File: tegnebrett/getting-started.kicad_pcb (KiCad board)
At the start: 2 copper layers, 15 parts, among them J1 FH12-45S-0.5SH55, J2 FH12-6S-1SH55, J3 Conn_ST_STDC14, J4 DA15_Socket, J5 MCU_Header_Pin, J6 FPGA_Header_Pin, J8 USB-A1HSW6, U1 XC7A100T-2FTG256I, U2 Oscillator 100MHz, U3 TPS54294PWP1, U4 TPS54294PWP2, U5 STM32U5G7VJTxQ, U6 VGA Transceiver, U7 VGA Transciever, U8 IS66WVH16M8DBLL-100B1LI1

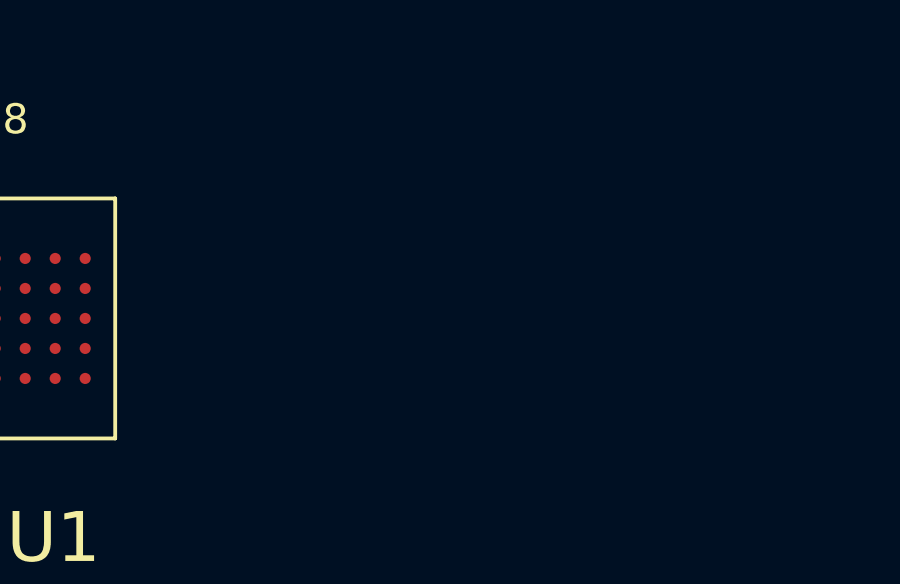
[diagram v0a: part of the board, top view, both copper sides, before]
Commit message: feat: add FPGA flash footprint, import to PCB
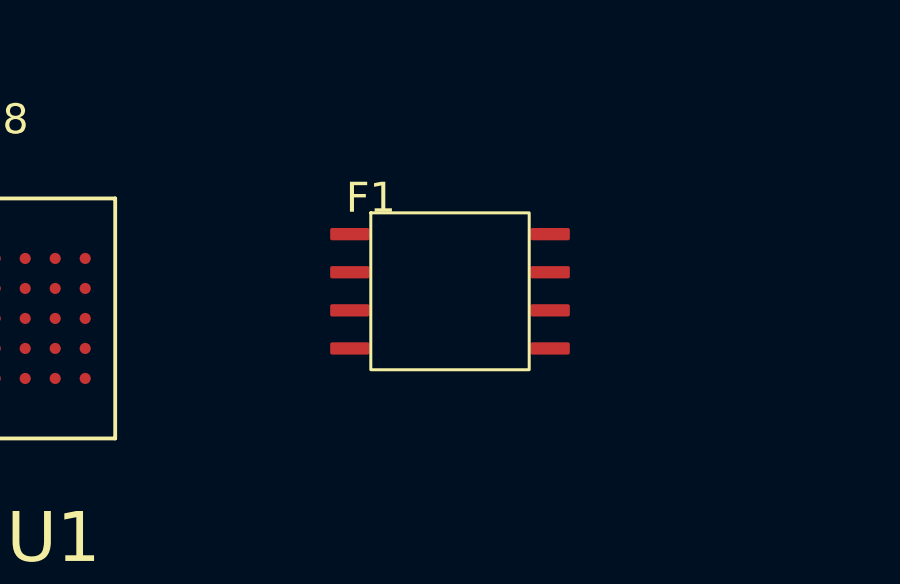
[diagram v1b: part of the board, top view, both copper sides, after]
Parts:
- added F1: GD25F128FS2GR1, tegnebrett_modules:flash_tegnebrett, F.Cu at (54.5, 18.0)
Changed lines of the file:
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@@
 	(net 205 "unconnected-(U1A-IO_L14P_T2_SRCC_14-PadP10)")
 	(net 206 "Net-(U1A-IO_L24P_T3_RS1_15)")
-	(net 207 "Net-(GD25F128FS2GR1-SCLK)")
+	(net 207 "Net-(F1-SI(IO0))")
 	(net 208 "Net-(U1C-TDO_0)")
-	(net 209 "Net-(GD25F128FS2GR1-IO3)")
+	(net 209 "Net-(F1-IO3)")
 	(net 210 "unconnected-(U1B-IO_L4N_T0_34-PadP1)")
 	(net 211 "unconnected-(U1B-IO_L6N_T0_VREF_34-PadN4)")
@@
 	(net 237 "unconnected-(U1B-IO_L22N_T3_35-PadJ1)")
 	(net 238 "unconnected-(U1B-IO_L2P_T0_34-PadM2)")
-	(net 239 "Net-(GD25F128FS2GR1-IO2)")
+	(net 239 "Net-(F1-SCLK)")
 	(net 240 "unconnected-(U1B-IO_L16N_T2_35-PadG4)")
 	(net 241 "unconnected-(U1B-IO_L13P_T2_MRCC_35-PadF5)")
@@
 	(net 249 "unconnected-(U1B-IO_L10P_T1_34-PadP5)")
 	(net 250 "unconnected-(U1A-IO_L3N_T0_DQS_EMCCLK_14-PadM15)")
-	(net 251 "Net-(GD25F128FS2GR1-SO1(IO1))")
+	(net 251 "Net-(F1-SO1(IO1))")
 	(net 252 "unconnected-(U1A-IO_L5P_T0_AD9P_15-PadB12)")
 	(net 253 "Net-(U1C-TMS_0)")
@@
 	(net 326 "Net-(U1C-INIT_B_0)")
 	(net 327 "unconnected-(U1A-IO_L8N_T1_AD10N_15-PadB14)")
-	(net 328 "Net-(GD25F128FS2GR1-SI(IO0))")
+	(net 328 "Net-(F1-IO2)")
 	(footprint "Connector_PinHeader_1.27mm:PinHeader_2x07_P1.27mm_Vertical"
 		(layer "F.Cu")
@@
 			(size 0.5 0.5)
 			(layers "F.Cu" "F.Mask" "F.Paste")
-			(net 207 "Net-(GD25F128FS2GR1-SCLK)")
+			(net 239 "Net-(F1-SCLK)")
 			(pinfunction "CCLK_0")
 			(pintype "bidirectional")
@@
 			(size 0.5 0.5)
 			(layers "F.Cu" "F.Mask" "F.Paste")
-			(net 328 "Net-(GD25F128FS2GR1-SI(IO0))")
+			(net 207 "Net-(F1-SI(IO0))")
 			(pinfunction "IO_L1P_T0_D00_MOSI_14")
 			(pintype "bidirectional")
@@
 			(size 0.5 0.5)
 			(layers "F.Cu" "F.Mask" "F.Paste")
-			(net 251 "Net-(GD25F128FS2GR1-SO1(IO1))")
+			(net 251 "Net-(F1-SO1(IO1))")
 			(pinfunction "IO_L1N_T0_D01_DIN_14")
 			(pintype "bidirectional")
@@
 			(size 0.5 0.5)
 			(layers "F.Cu" "F.Mask" "F.Paste")
-			(net 239 "Net-(GD25F128FS2GR1-IO2)")
+			(net 328 "Net-(F1-IO2)")
 			(pinfunction "IO_L2P_T0_D02_14")
 			(pintype "bidirectional")
@@
 			(size 0.5 0.5)
 			(layers "F.Cu" "F.Mask" "F.Paste")
-			(net 209 "Net-(GD25F128FS2GR1-IO3)")
+			(net 209 "Net-(F1-IO3)")
 			(pinfunction "IO_L2N_T0_D03_14")
 			(pintype "bidirectional")
@@
 		)
 	)
+	(footprint "tegnebrett_modules:flash_tegnebrett"
+		(layer "F.Cu")
+		(at 54.52 17.98)
+		(property "Reference" "F1"
+			(at 0 -0.5 0)
+			(unlocked yes)
+			(layer "F.SilkS")
+			(effects
+				(font
+					(size 1 1)
+					(thickness 0.1)
+				)
+			)
+		)
+		(property "Value" "GD25F128FS2GR1"
+			(at 0 1 0)
+			(unlocked yes)
+			(layer "F.Fab")
+			(effects
+				(font
+					(size 1 1)
+					(thickness 0.15)
+				)
+			)
+		)
+		(property "Datasheet" ""
+			(at 0 0 0)
+			(unlocked yes)
+			(layer "F.Fab")
+			(hide yes)
+			(effects
+				(font
+					(size 1 1)
+					(thickness 0.15)
+				)
+			)
+		)
+		(property "Description" ""
+			(at 0 0 0)
+			(unlocked yes)
+			(layer "F.Fab")
+			(hide yes)
+			(effects
+				(font
+					(size 1 1)
+					(thickness 0.15)
+				)
+			)
+		)
+		(sheetname "/FPGA/")
+		(sheetfile "debug.kicad_sch")
+		(attr smd)
+		(fp_rect
+			(start 0 0)
+			(end 5.28 5.23)
+			(stroke
+				(width 0.1)
+				(type solid)
+			)
+			(fill no)
+			(layer "F.SilkS")
+		)
+		(fp_text user "${REFERENCE}"
+			(at 0 2.5 0)
+			(unlocked yes)
+			(layer "F.Fab")
+			(effects
+				(font
+					(size 1 1)
+					(thickness 0.15)
+				)
+			)
+		)
+		(pad "1" smd roundrect
+			(at -0.7 0.71)
+			(size 1.31 0.41)
+			(layers "F.Cu" "F.Mask" "F.Paste")
+			(roundrect_rratio 0.15)
+			(net 302 "/FPGA/CS#")
+			(pinfunction "CS#")
+			(pintype "input")
+		)
+		(pad "2" smd roundrect
+			(at -0.7 1.98)
+			(size 1.31 0.41)
+			(layers "F.Cu" "F.Mask" "F.Paste")
+			(roundrect_rratio 0.15)
+			(net 251 "Net-(F1-SO1(IO1))")
+			(pinfunction "SO1(IO1)")
+			(pintype "bidirectional")
+		)
+		(pad "3" smd roundrect
+			(at -0.7 3.25)
+			(size 1.31 0.41)
+			(layers "F.Cu" "F.Mask" "F.Paste")
+			(roundrect_rratio 0.15)
+			(net 328 "Net-(F1-IO2)")
+			(pinfunction "IO2")
+			(pintype "bidirectional")
+		)
+		(pad "4" smd roundrect
+			(at -0.7 4.52)
+			(size 1.31 0.41)
+			(layers "F.Cu" "F.Mask" "F.Paste")
+			(roundrect_rratio 0.15)
+			(net 1 "GND")
+			(pinfunction "VSS")
+			(pintype "power_in")
+		)
+		(pad "5" smd roundrect
+			(at 5.98 4.52)
+			(size 1.31 0.41)
+			(layers "F.Cu" "F.Mask" "F.Paste")
+			(roundrect_rratio 0.15)
+			(net 207 "Net-(F1-SI(IO0))")
+			(pinfunction "SI(IO0)")
+			(pintype "bidirectional")
+		)
+		(pad "6" smd roundrect
+			(at 5.98 3.25)
+			(size 1.31 0.41)
+			(layers "F.Cu" "F.Mask" "F.Paste")
+			(roundrect_rratio 0.15)
+			(net 239 "Net-(F1-SCLK)")
+			(pinfunction "SCLK")
+			(pintype "input")
+		)
+		(pad "7" smd roundrect
+			(at 5.98 1.98)
+			(size 1.31 0.41)
+			(layers "F.Cu" "F.Mask" "F.Paste")
+			(roundrect_rratio 0.15)
+			(net 209 "Net-(F1-IO3)")
+			(pinfunction "IO3")
+			(pintype "bidirectional")
+		)
+		(pad "8" smd roundrect
+			(at 5.98 0.71)
+			(size 1.31 0.41)
+			(layers "F.Cu" "F.Mask" "F.Paste")
+			(roundrect_rratio 0.15)
+			(net 16 "+3V3")
+			(pinfunction "VCC")
+			(pintype "power_in")
+		)
+		(embedded_fonts no)
+	)
 	(footprint "tegnebrett_modules:psram"

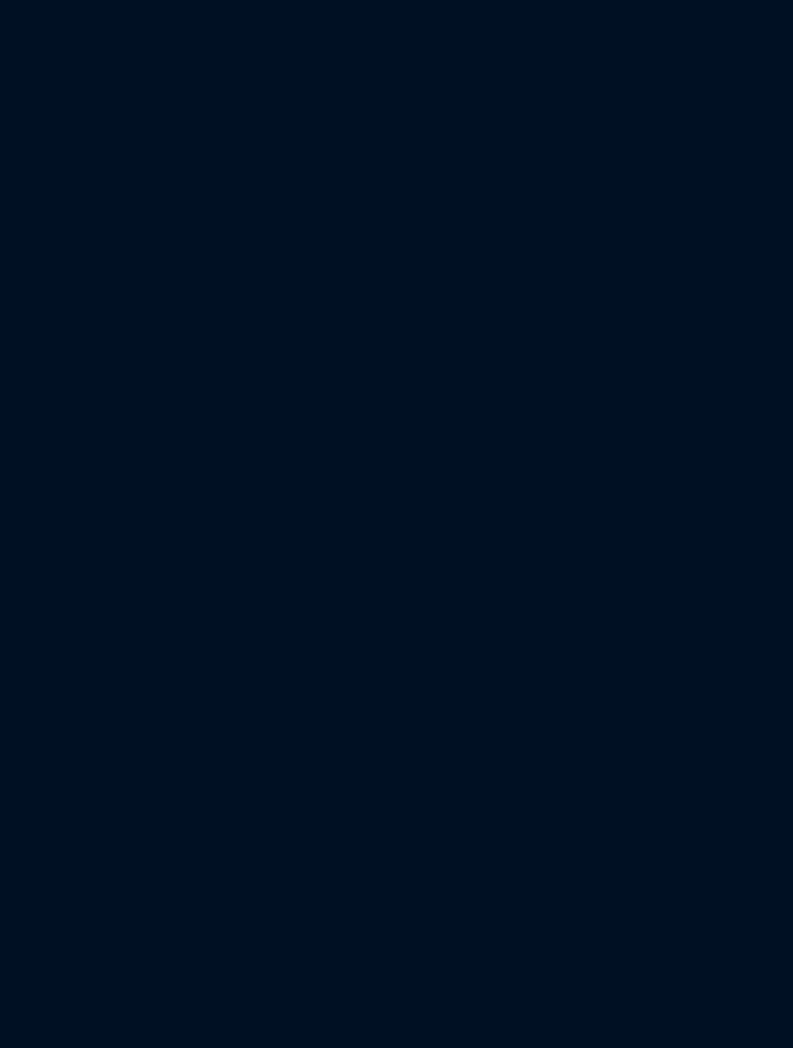
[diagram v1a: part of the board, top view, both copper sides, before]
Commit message: feat: add LED footprint, and add them to PCB
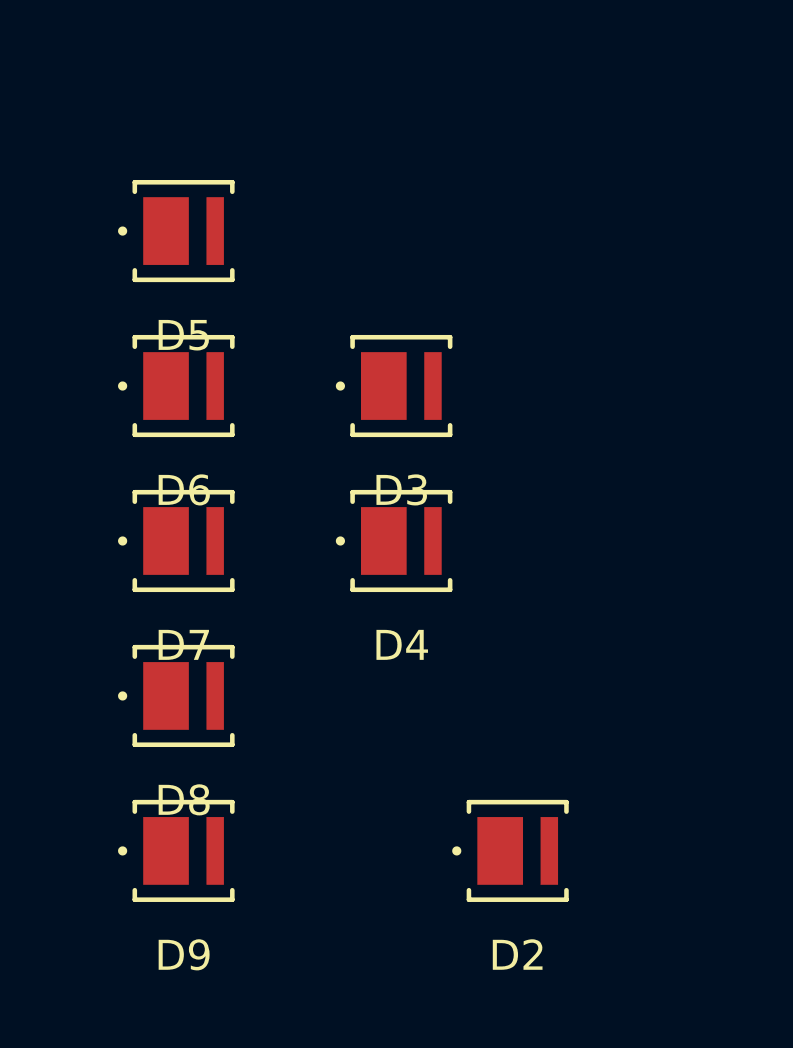
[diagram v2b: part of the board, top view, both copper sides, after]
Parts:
- added D2: LED, tegnebrett_modules:LED_J-SERIES_3030_CRW-M, F.Cu at (28.6, 192.5)
- added D3: LED, tegnebrett_modules:LED_J-SERIES_3030_CRW-M, F.Cu at (24.7, 177.0)
- added D4: LED, tegnebrett_modules:LED_J-SERIES_3030_CRW-M, F.Cu at (24.7, 182.2)
- added D5: LED, tegnebrett_modules:LED_J-SERIES_3030_CRW-M, F.Cu at (17.4, 171.8)
- added D6: LED, tegnebrett_modules:LED_J-SERIES_3030_CRW-M, F.Cu at (17.4, 177.0)
- added D7: LED, tegnebrett_modules:LED_J-SERIES_3030_CRW-M, F.Cu at (17.4, 182.2)
- added D8: LED, tegnebrett_modules:LED_J-SERIES_3030_CRW-M, F.Cu at (17.4, 187.3)
- added D9: LED, tegnebrett_modules:LED_J-SERIES_3030_CRW-M, F.Cu at (17.4, 192.5)

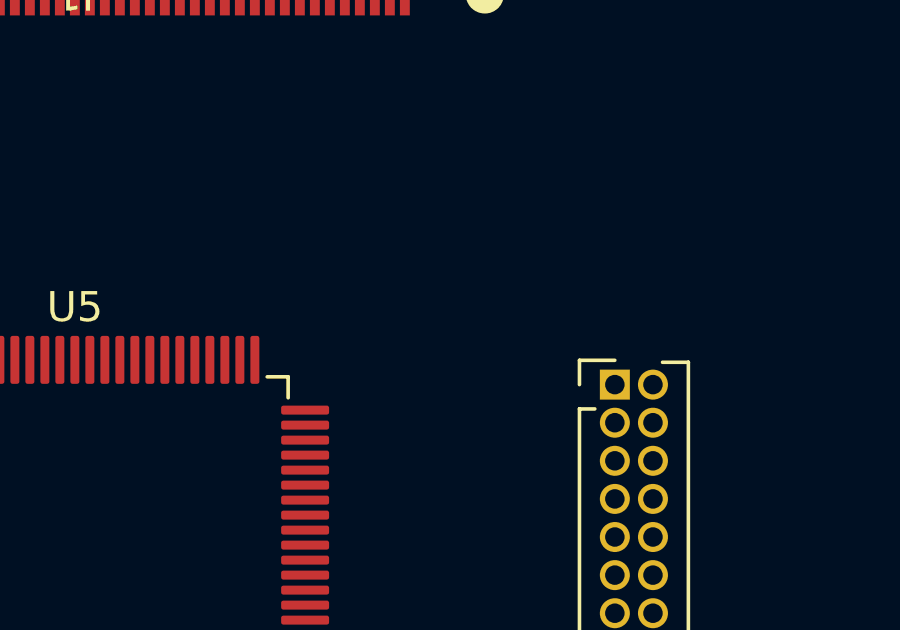
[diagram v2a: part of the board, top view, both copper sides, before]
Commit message: feat: add 48MHz crystal footprint + add to PCB
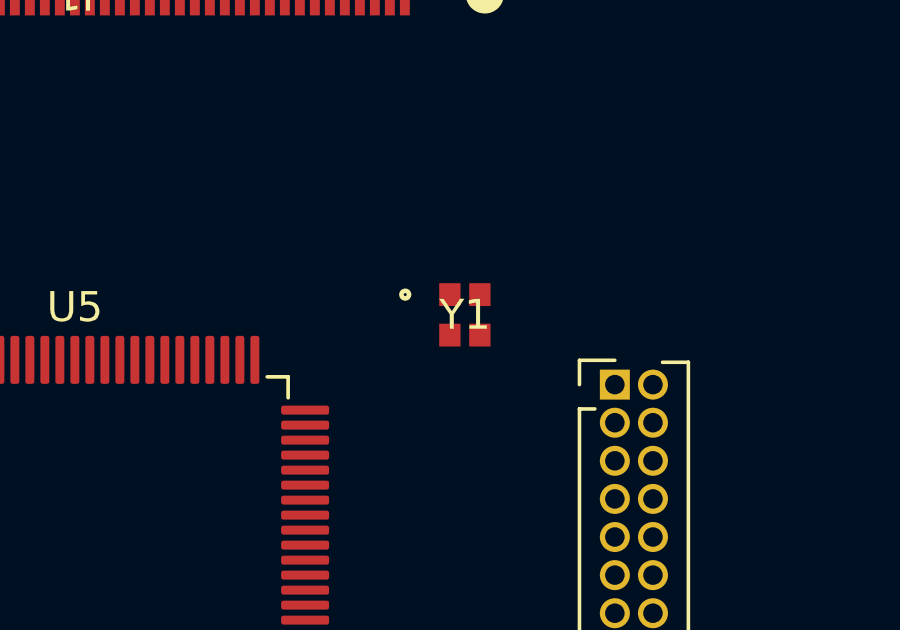
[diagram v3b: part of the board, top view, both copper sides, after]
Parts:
- added Y1: 48MHz, tegnebrett_modules:XRCGB48M000F4M00R0_MUR, F.Cu at (211.5, 112.8)

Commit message: feat: add inductors and capacitors to PCB
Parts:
- added C1: 47u, Capacitor_SMD:C_0805_2012Metric_Pad1.18x1.45mm_HandSolder, F.Cu at (123.3, 146.9)
- added C10: 4u7, Capacitor_SMD:C_0805_2012Metric_Pad1.18x1.45mm_HandSolder, F.Cu at (123.3, 162.0)
- added C100: 100n, Capacitor_SMD:C_0805_2012Metric_Pad1.18x1.45mm_HandSolder, F.Cu at (150.6, 168.0)
- added C101: 22u, Capacitor_SMD:C_1206_3216Metric_Pad1.33x1.80mm_HandSolder, F.Cu at (162.0, 153.8)
- added C102: 22u, Capacitor_SMD:C_1206_3216Metric_Pad1.33x1.80mm_HandSolder, F.Cu at (162.0, 157.2)
- added C103: 22u, Capacitor_SMD:C_1206_3216Metric_Pad1.33x1.80mm_HandSolder, F.Cu at (162.0, 160.5)
- added C104: 10u, Capacitor_SMD:C_1206_3216Metric_Pad1.33x1.80mm_HandSolder, F.Cu at (162.0, 163.8)
- added C105: 10u, Capacitor_SMD:C_1206_3216Metric_Pad1.33x1.80mm_HandSolder, F.Cu at (162.0, 167.2)
- added C11: 4u7, Capacitor_SMD:C_0805_2012Metric_Pad1.18x1.45mm_HandSolder, F.Cu at (123.3, 165.0)
- added C12: 470n, Capacitor_SMD:C_0805_2012Metric_Pad1.18x1.45mm_HandSolder, F.Cu at (123.3, 168.0)
- added C13: 4u7, Capacitor_SMD:C_0805_2012Metric_Pad1.18x1.45mm_HandSolder, F.Cu at (123.3, 171.0)
- added C14: 10u, Capacitor_SMD:C_1206_3216Metric_Pad1.33x1.80mm_HandSolder, F.Cu at (156.0, 153.8)
- added C15: 4u7, Capacitor_SMD:C_0805_2012Metric_Pad1.18x1.45mm_HandSolder, F.Cu at (128.2, 146.9)
- added C16: 4u7, Capacitor_SMD:C_0805_2012Metric_Pad1.18x1.45mm_HandSolder, F.Cu at (128.2, 149.9)
- added C17: 4u7, Capacitor_SMD:C_0805_2012Metric_Pad1.18x1.45mm_HandSolder, F.Cu at (128.2, 152.9)
- added C18: 470n, Capacitor_SMD:C_0805_2012Metric_Pad1.18x1.45mm_HandSolder, F.Cu at (128.2, 156.0)
- added C19: 470n, Capacitor_SMD:C_0805_2012Metric_Pad1.18x1.45mm_HandSolder, F.Cu at (128.2, 159.0)
- added C2: 10u, Capacitor_SMD:C_1206_3216Metric_Pad1.33x1.80mm_HandSolder, F.Cu at (156.0, 147.1)
- added C20: 22u, Capacitor_SMD:C_1206_3216Metric_Pad1.33x1.80mm_HandSolder, F.Cu at (156.0, 157.2)
- added C21: 470n, Capacitor_SMD:C_0805_2012Metric_Pad1.18x1.45mm_HandSolder, F.Cu at (128.2, 162.0)
- added C22: 4u7, Capacitor_SMD:C_0805_2012Metric_Pad1.18x1.45mm_HandSolder, F.Cu at (128.2, 165.0)
- added C23: 470n, Capacitor_SMD:C_0805_2012Metric_Pad1.18x1.45mm_HandSolder, F.Cu at (128.2, 168.0)
- added C24: 470n, Capacitor_SMD:C_0805_2012Metric_Pad1.18x1.45mm_HandSolder, F.Cu at (128.2, 171.0)
- added C25: 100n, Capacitor_SMD:C_0805_2012Metric_Pad1.18x1.45mm_HandSolder, F.Cu at (150.6, 146.9)
- added C26: 470n, Capacitor_SMD:C_0805_2012Metric_Pad1.18x1.45mm_HandSolder, F.Cu at (133.0, 146.9)
- added C27: 4u7, Capacitor_SMD:C_0805_2012Metric_Pad1.18x1.45mm_HandSolder, F.Cu at (133.0, 149.9)
- added C28: 470n, Capacitor_SMD:C_0805_2012Metric_Pad1.18x1.45mm_HandSolder, F.Cu at (133.0, 152.9)
- added C29: 470n, Capacitor_SMD:C_0805_2012Metric_Pad1.18x1.45mm_HandSolder, F.Cu at (133.0, 156.0)
- added C3: 47u, Capacitor_SMD:C_0805_2012Metric_Pad1.18x1.45mm_HandSolder, F.Cu at (123.3, 149.9)
- added C30: 100n, Capacitor_SMD:C_0805_2012Metric_Pad1.18x1.45mm_HandSolder, F.Cu at (150.6, 149.9)
- added C31: 470n, Capacitor_SMD:C_0805_2012Metric_Pad1.18x1.45mm_HandSolder, F.Cu at (133.0, 159.0)
- added C32: 4u7, Capacitor_SMD:C_0805_2012Metric_Pad1.18x1.45mm_HandSolder, F.Cu at (133.0, 162.0)
- added C33: 470n, Capacitor_SMD:C_0805_2012Metric_Pad1.18x1.45mm_HandSolder, F.Cu at (133.0, 165.0)
- added C34: 470n, Capacitor_SMD:C_0805_2012Metric_Pad1.18x1.45mm_HandSolder, F.Cu at (133.0, 168.0)
- added C35: 100n, Capacitor_SMD:C_0805_2012Metric_Pad1.18x1.45mm_HandSolder, F.Cu at (150.6, 152.9)
- added C36: 470n, Capacitor_SMD:C_0805_2012Metric_Pad1.18x1.45mm_HandSolder, F.Cu at (133.0, 171.0)
- added C37: 4u7, Capacitor_SMD:C_0805_2012Metric_Pad1.18x1.45mm_HandSolder, F.Cu at (137.8, 146.9)
- added C38: 470n, Capacitor_SMD:C_0805_2012Metric_Pad1.18x1.45mm_HandSolder, F.Cu at (137.8, 149.9)
- added C39: 470n, Capacitor_SMD:C_0805_2012Metric_Pad1.18x1.45mm_HandSolder, F.Cu at (137.8, 152.9)
- added C4: 330u, Capacitor_SMD:C_1210_3225Metric_Pad1.33x2.70mm_HandSolder, F.Cu at (143.2, 150.9)
- added C40: 470n, Capacitor_SMD:C_0805_2012Metric_Pad1.18x1.45mm_HandSolder, F.Cu at (137.8, 156.0)
- added C41: 470n, Capacitor_SMD:C_0805_2012Metric_Pad1.18x1.45mm_HandSolder, F.Cu at (137.8, 159.0)
- added C42: 470n, Capacitor_SMD:C_0805_2012Metric_Pad1.18x1.45mm_HandSolder, F.Cu at (137.8, 162.0)
- added C43: 470n, Capacitor_SMD:C_0805_2012Metric_Pad1.18x1.45mm_HandSolder, F.Cu at (137.8, 165.0)
- added C44: 470n, Capacitor_SMD:C_0805_2012Metric_Pad1.18x1.45mm_HandSolder, F.Cu at (137.8, 168.0)
- added C45: 470n, Capacitor_SMD:C_0805_2012Metric_Pad1.18x1.45mm_HandSolder, F.Cu at (137.8, 171.0)
- added C46: 47u, Capacitor_SMD:C_0805_2012Metric_Pad1.18x1.45mm_HandSolder, F.Cu at (150.6, 173.0)
- added C47: 100n, Capacitor_SMD:C_0805_2012Metric_Pad1.18x1.45mm_HandSolder, F.Cu at (150.6, 176.0)
- added C48: 100n, Capacitor_SMD:C_0805_2012Metric_Pad1.18x1.45mm_HandSolder, F.Cu at (150.6, 179.0)
- added C49: 100n, Capacitor_SMD:C_0805_2012Metric_Pad1.18x1.45mm_HandSolder, F.Cu at (150.6, 182.0)
- added C5: 47u, Capacitor_SMD:C_0805_2012Metric_Pad1.18x1.45mm_HandSolder, F.Cu at (123.3, 152.9)
- added C50: 100n, Capacitor_SMD:C_0805_2012Metric_Pad1.18x1.45mm_HandSolder, F.Cu at (150.6, 185.1)
- added C51: 100n, Capacitor_SMD:C_0805_2012Metric_Pad1.18x1.45mm_HandSolder, F.Cu at (150.6, 188.1)
- added C6: 100u, Capacitor_SMD:C_1206_3216Metric_Pad1.33x1.80mm_HandSolder, F.Cu at (143.2, 147.1)
- added C7: 4u7, Capacitor_SMD:C_0805_2012Metric_Pad1.18x1.45mm_HandSolder, F.Cu at (123.3, 156.0)
- added C71: 6p, Capacitor_SMD:C_0805_2012Metric_Pad1.18x1.45mm_HandSolder, F.Cu at (123.3, 176.0)
- added C72: 6p, Capacitor_SMD:C_0805_2012Metric_Pad1.18x1.45mm_HandSolder, F.Cu at (123.3, 179.0)
- added C73: 1µ, Capacitor_SMD:C_0805_2012Metric_Pad1.18x1.45mm_HandSolder, F.Cu at (123.3, 182.0)
- added C74: 100n, Capacitor_SMD:C_0805_2012Metric_Pad1.18x1.45mm_HandSolder, F.Cu at (123.3, 185.1)
- added C75: 100n, Capacitor_SMD:C_0805_2012Metric_Pad1.18x1.45mm_HandSolder, F.Cu at (123.3, 188.1)
- added C76: 100n, Capacitor_SMD:C_0805_2012Metric_Pad1.18x1.45mm_HandSolder, F.Cu at (128.2, 176.0)
- added C77: 100n, Capacitor_SMD:C_0805_2012Metric_Pad1.18x1.45mm_HandSolder, F.Cu at (128.2, 179.0)
- added C78: 100n, Capacitor_SMD:C_0805_2012Metric_Pad1.18x1.45mm_HandSolder, F.Cu at (128.2, 182.0)
- added C79: 10µ, Capacitor_SMD:C_1206_3216Metric_Pad1.33x1.80mm_HandSolder, F.Cu at (138.4, 176.2)
- added C8: 10u, Capacitor_SMD:C_1206_3216Metric_Pad1.33x1.80mm_HandSolder, F.Cu at (156.0, 150.4)
- added C80: 100n, Capacitor_SMD:C_0805_2012Metric_Pad1.18x1.45mm_HandSolder, F.Cu at (128.2, 185.1)
- added C81: 100n, Capacitor_SMD:C_0805_2012Metric_Pad1.18x1.45mm_HandSolder, F.Cu at (128.2, 188.1)
- added C82: 2.2µ, Capacitor_SMD:C_0805_2012Metric_Pad1.18x1.45mm_HandSolder, F.Cu at (133.0, 176.0)
- added C83: 10µ, Capacitor_SMD:C_1206_3216Metric_Pad1.33x1.80mm_HandSolder, F.Cu at (138.4, 179.5)
- added C84: 2.2µ, Capacitor_SMD:C_0805_2012Metric_Pad1.18x1.45mm_HandSolder, F.Cu at (133.0, 179.0)
- added C85: 100n, Capacitor_SMD:C_0805_2012Metric_Pad1.18x1.45mm_HandSolder, F.Cu at (133.0, 182.0)
- added C86: 1µ, Capacitor_SMD:C_0805_2012Metric_Pad1.18x1.45mm_HandSolder, F.Cu at (133.0, 185.1)
- added C87: 1u, Capacitor_SMD:C_0805_2012Metric_Pad1.18x1.45mm_HandSolder, F.Cu at (157.4, 173.0)
- added C88: 1u, Capacitor_SMD:C_0805_2012Metric_Pad1.18x1.45mm_HandSolder, F.Cu at (157.4, 176.0)
- added C89: 100n, Capacitor_SMD:C_0805_2012Metric_Pad1.18x1.45mm_HandSolder, F.Cu at (157.4, 179.0)
- added C9: 4u7, Capacitor_SMD:C_0805_2012Metric_Pad1.18x1.45mm_HandSolder, F.Cu at (123.3, 159.0)
- added C90: 100n, Capacitor_SMD:C_0805_2012Metric_Pad1.18x1.45mm_HandSolder, F.Cu at (157.4, 182.0)
- added C91: 22u, Capacitor_SMD:C_1206_3216Metric_Pad1.33x1.80mm_HandSolder, F.Cu at (156.0, 160.5)
- added C92: 22u, Capacitor_SMD:C_1206_3216Metric_Pad1.33x1.80mm_HandSolder, F.Cu at (156.0, 163.8)
- added C93: 1u, Capacitor_SMD:C_0805_2012Metric_Pad1.18x1.45mm_HandSolder, F.Cu at (150.6, 156.0)
- added C94: 100n, Capacitor_SMD:C_0805_2012Metric_Pad1.18x1.45mm_HandSolder, F.Cu at (150.6, 159.0)
- added C95: 22u, Capacitor_SMD:C_1206_3216Metric_Pad1.33x1.80mm_HandSolder, F.Cu at (156.0, 167.2)
- added C96: 22u, Capacitor_SMD:C_1206_3216Metric_Pad1.33x1.80mm_HandSolder, F.Cu at (162.0, 147.1)
- added C97: 1u, Capacitor_SMD:C_0805_2012Metric_Pad1.18x1.45mm_HandSolder, F.Cu at (150.6, 162.0)
- added C98: 100n, Capacitor_SMD:C_0805_2012Metric_Pad1.18x1.45mm_HandSolder, F.Cu at (150.6, 165.0)
- added C99: 10u, Capacitor_SMD:C_1206_3216Metric_Pad1.33x1.80mm_HandSolder, F.Cu at (162.0, 150.4)
- added L4: 2.2µ, Inductor_SMD:L_0805_2012Metric_Pad1.15x1.40mm_HandSolder, F.Cu at (52.0, 194.6)
- added L5: 1.5u, Inductor_SMD:L_0805_2012Metric_Pad1.15x1.40mm_HandSolder, F.Cu at (47.0, 185.6)
- added L6: 1.5u, Inductor_SMD:L_0805_2012Metric_Pad1.15x1.40mm_HandSolder, F.Cu at (47.0, 188.6)
- added L7: 2u2, Inductor_SMD:L_0805_2012Metric_Pad1.15x1.40mm_HandSolder, F.Cu at (47.0, 191.5)
- added L8: 3u3, Inductor_SMD:L_0805_2012Metric_Pad1.15x1.40mm_HandSolder, F.Cu at (47.0, 194.4)
- moved J1 54.4 mm to (250.5, 114.5)
- moved J2 54.4 mm to (229.0, 115.0)
- moved J3 54.4 mm to (268.5, 131.2)
- moved J5 54.4 mm to (242.4, 155.0)
- moved J8 54.4 mm to (228.8, 136.7)
- moved U5 54.4 mm to (250.5, 138.0)
- moved Y1 54.4 mm to (263.5, 128.8)
- moved D4 5.34 mm to (25.0, 187.5)
- moved D3 5.01 mm to (25.0, 182.0)
- moved D2 3.50 mm to (25.1, 192.5)
